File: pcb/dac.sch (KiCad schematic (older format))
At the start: 83 parts, among them U6 MAX5853ETL-T, U7 TLV3542IDR

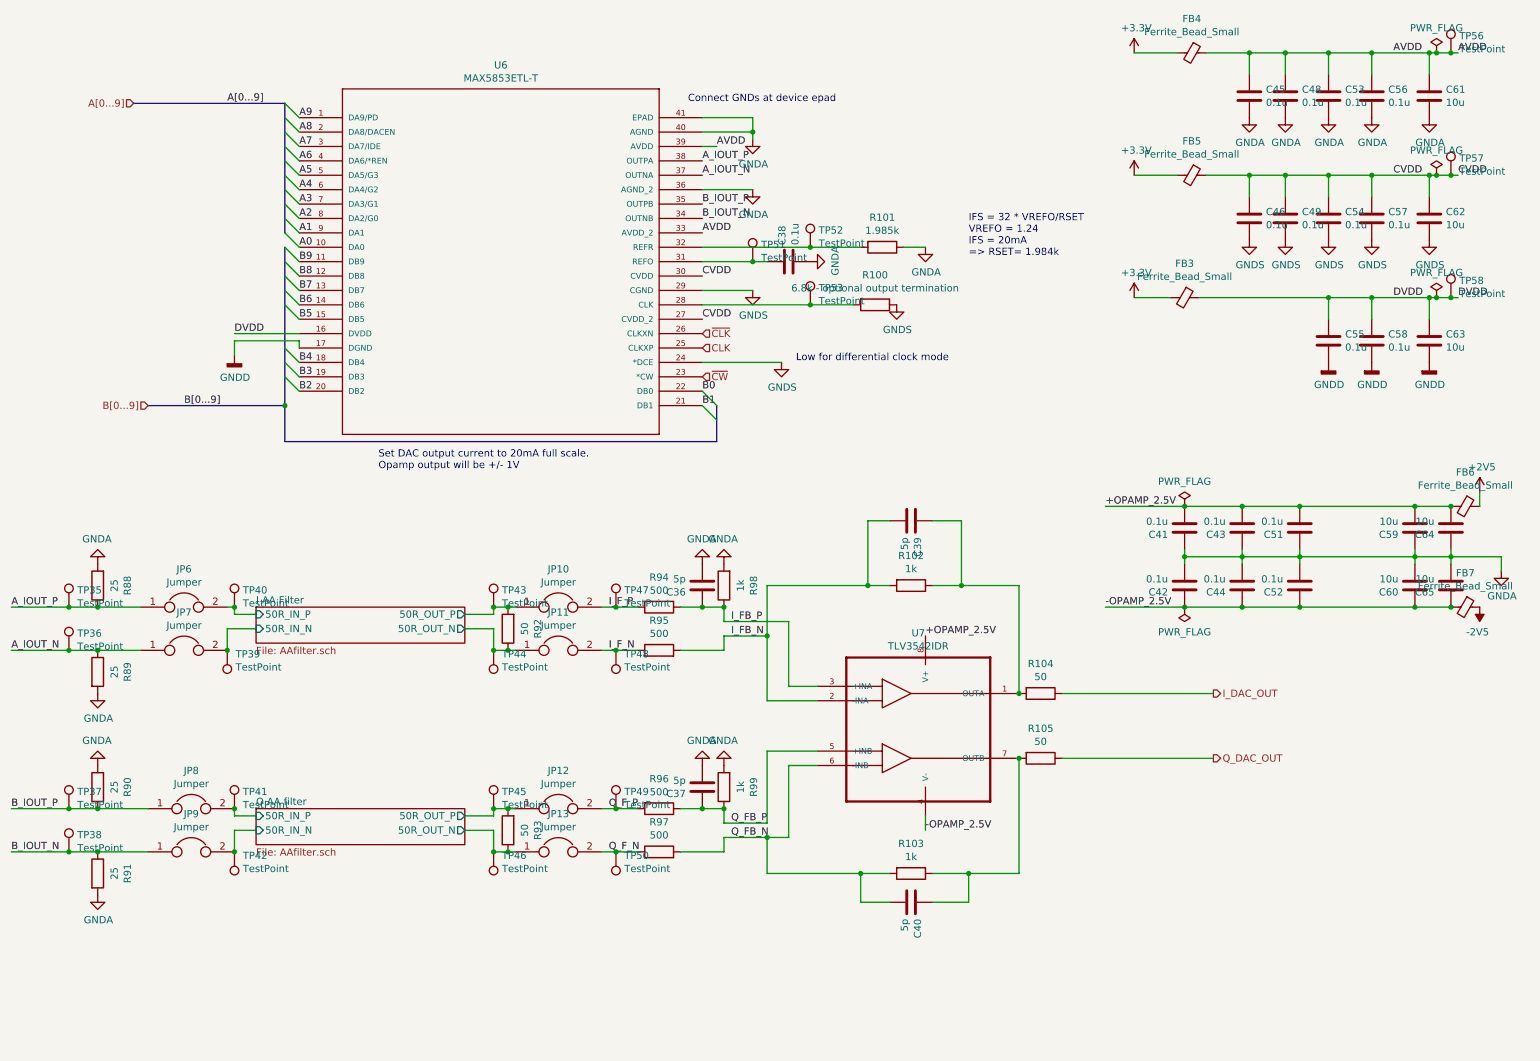
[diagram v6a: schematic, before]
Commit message: LO amp routing
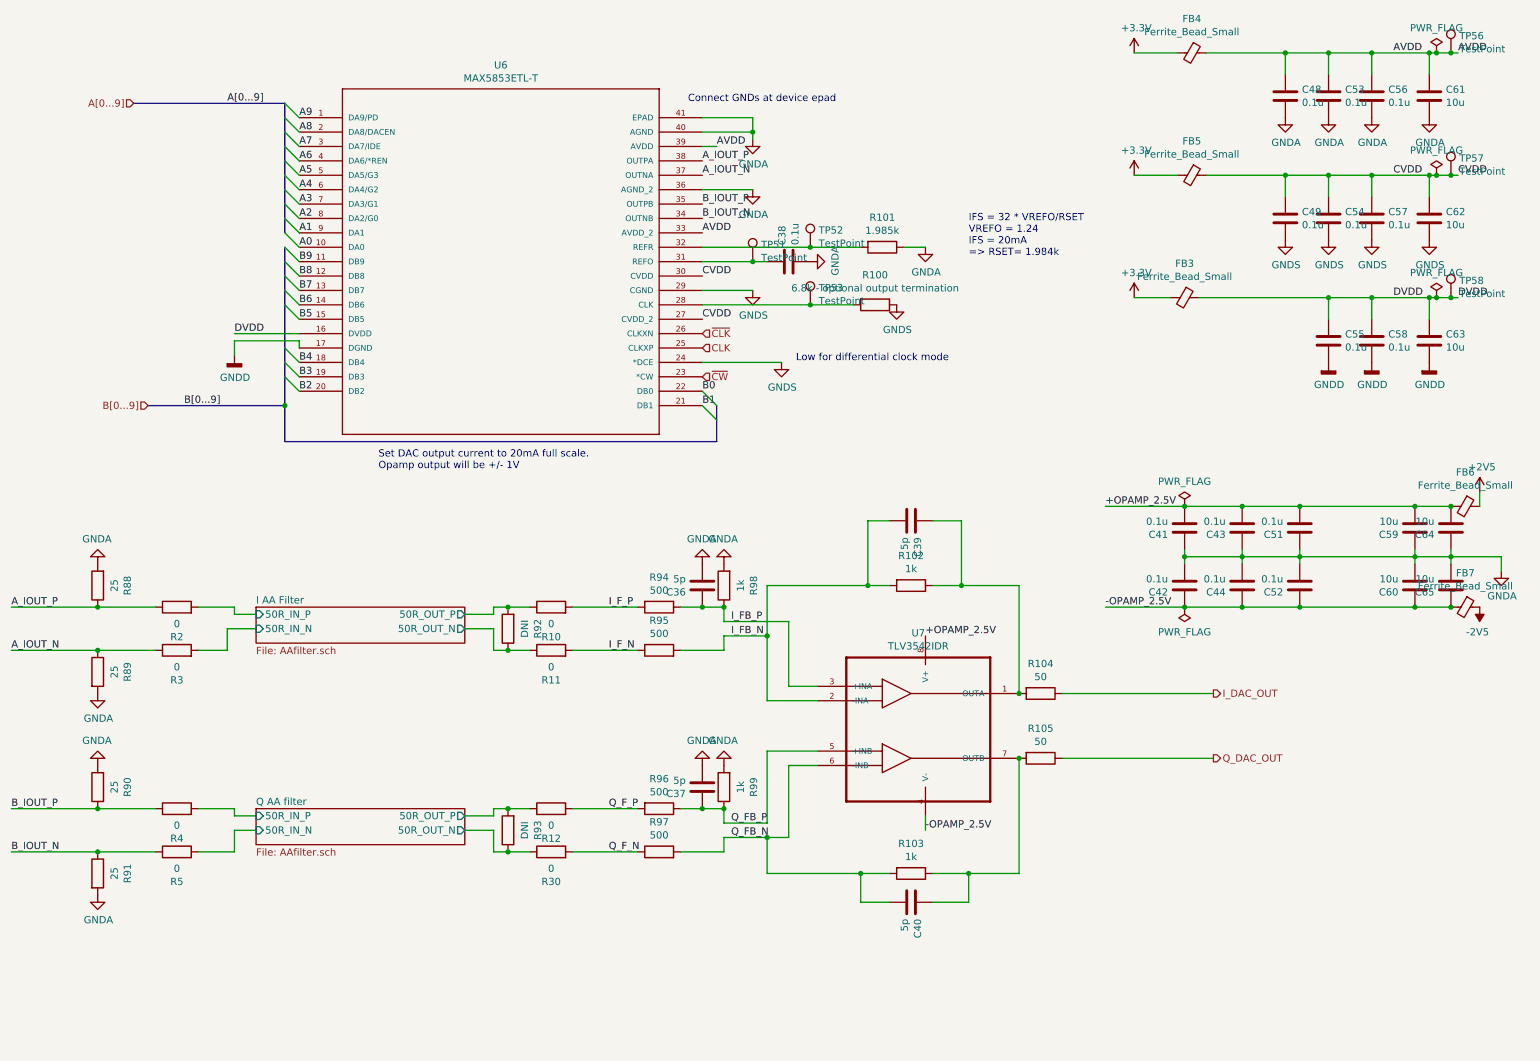
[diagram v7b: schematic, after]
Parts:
- removed C45, C46: 0.1u, Capacitor_SMD:C_0603_1608Metric, symbol Device:C
- removed JP10, JP11, JP12, JP13, JP6, JP7, JP8, JP9: Jumper, Resistor_SMD:R_0603_1608Metric, symbol Device:Jumper
- removed TP35, TP36, TP37, TP38, TP39, TP40, TP41, TP42, TP43, TP44, TP45, TP46, TP47, TP48, TP49, TP50: TestPoint, TestPoint:TestPoint_Pad_D1.5mm, symbol Connector:TestPoint
- added R10, R11, R12, R2, R3, R30, R4, R5: 0, Resistor_SMD:R_0603_1608Metric, symbol Device:R
- R92, R93: value 50 -> DNI
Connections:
- net A_IOUT_N: now also R3.1
- net A_IOUT_P: now also R2.1
- net B_IOUT_N: now also R5.1
- net B_IOUT_P: now also R4.1
- net I AA Filter/50R_IN_N: now also R3.2
- net I AA Filter/50R_IN_P: now also R2.2
- net I AA Filter/50R_OUT_N: now also R11.1
- net I AA Filter/50R_OUT_P: now also R10.1
- net I_F_N: now also R11.2
- net I_F_P: now also R10.2
- net Q AA filter/50R_IN_N: now also R5.2
- net Q AA filter/50R_IN_P: now also R4.2
- net Q AA filter/50R_OUT_N: now also R30.1
- net Q AA filter/50R_OUT_P: now also R12.1
- net Q_F_N: now also R30.2
- net Q_F_P: now also R12.2
